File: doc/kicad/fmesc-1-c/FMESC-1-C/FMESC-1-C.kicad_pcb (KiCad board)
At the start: 2 copper layers, 14 x 21 mm, 33 parts, among them J1 Conn_01x02, J2 Conn_01x02, J3 Conn_01x02, J4 Conn_01x02, J5 Conn_01x02, J6 Conn_01x02, U1 FD6288Q

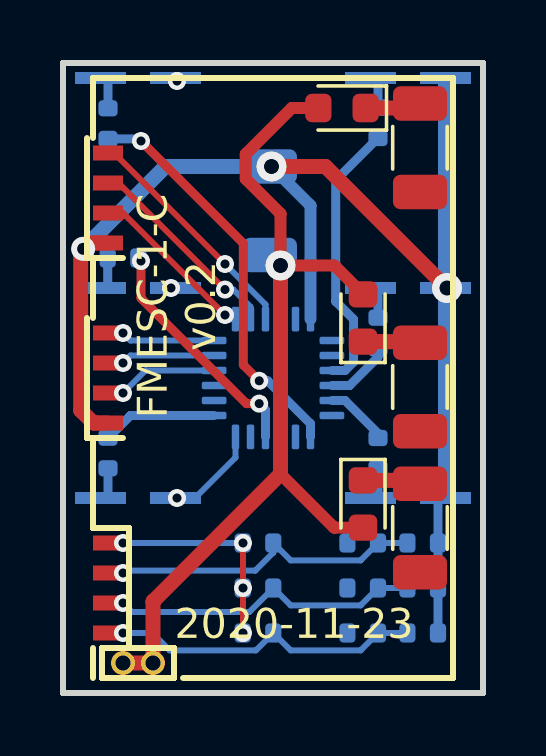
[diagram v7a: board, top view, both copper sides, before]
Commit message: doc/kicad: FMESC-1-C PCB clean and use FMPCBVDL-1
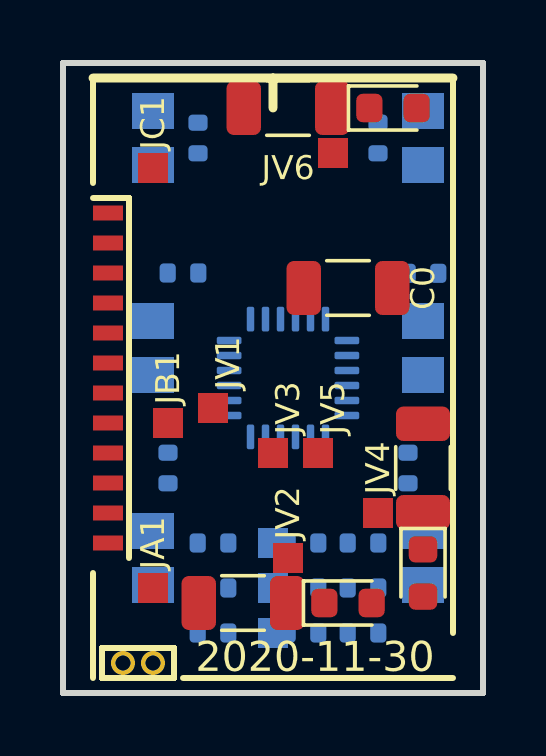
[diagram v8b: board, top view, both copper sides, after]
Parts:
- removed JC3: Conn_01x04, fmlibf:JS_4P_1.0mm
- added JA1: Conn_01x01, fmlibf:JS_1P_1x1mm, F.Cu at (116.5, 71.5)
- added JA2: Conn_01x01, fmlibf:JS_1P_1x1mm, B.Cu at (120.5, 73.0)
- added JB1: Conn_01x01, fmlibf:JS_1P_1x1mm, F.Cu at (117.0, 66.0)
- added JB2: Conn_01x01, fmlibf:JS_1P_1x1mm, B.Cu at (120.5, 71.5)
- added JM1: Conn_01x12, fmlibf:JS_12P_1.0mm, F.Cu at (115.0, 64.5)
- added JV1: Conn_01x01, fmlibf:JS_1P_1x1mm, F.Cu at (118.5, 65.5)
- added JV2: Conn_01x01, fmlibf:JS_1P_1x1mm, F.Cu at (121.0, 70.5)
- added JV3: Conn_01x01, fmlibf:JS_1P_1x1mm, F.Cu at (120.5, 67.0)
- added JV4: Conn_01x01, fmlibf:JS_1P_1x1mm, F.Cu at (124.0, 69.0)
- added JV5: Conn_01x01, fmlibf:JS_1P_1x1mm, F.Cu at (122.0, 67.0)
- added JV6: Conn_01x01, fmlibf:JS_1P_1x1mm, F.Cu at (122.5, 57.0)
- C0: moved to F.Cu
- J1, J2, J3, J4, J5, J6: footprint fmlibf:JS_2P_1.0mm_2 -> fmlibf:FMPCBVDL-1-S
- JC1: value Conn_01x04 -> Conn_01x01; footprint fmlibf:JS_4P_1.0mm -> fmlibf:JS_1P_1x1mm
- JC2: value Conn_01x04 -> Conn_01x01; footprint fmlibf:JS_4P_1.0mm -> fmlibf:JS_1P_1x1mm; moved to B.Cu
- moved D2 8.73 mm to (125.5, 71.0), turned to 270 degrees
- moved JC2 7.78 mm to (120.5, 70.0), turned to 0 degrees
- moved C1 6.41 mm to (119.5, 72.0), turned to 180 degrees
- moved C3 4.60 mm to (121.0, 55.5), turned to 180 degrees
- moved C0 3.66 mm to (123.0, 61.5), turned to 180 degrees
- moved R11 3.60 mm to (123.5, 73.0)
- moved R12 3.60 mm to (121.5, 73.0)
- moved R15 3.60 mm to (123.5, 70.0)
- moved R16 3.60 mm to (121.5, 70.0)
- moved R21 3.35 mm to (118.5, 73.0)
- moved R23 3.35 mm to (118.5, 70.0)
- moved D1 3.34 mm to (123.0, 72.0), turned to 0 degrees
- moved R6 3.04 mm to (118.0, 56.5)
- moved C2 2.70 mm to (125.5, 67.5), turned to 90 degrees
- moved R3 2.49 mm to (125.5, 61.0), turned to 0 degrees
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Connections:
- JC1 pad 1: GND -> /C1
- JC2 pad 1: GND -> Net-(JC2-Pad1)
- R12 pad 2: /A1 -> Net-(JA2-Pad1)
- R14 pad 2: /B1 -> Net-(JB2-Pad1)
- R16 pad 2: /C1 -> Net-(JC2-Pad1)
- U1 pad 1: /CAL1 -> /GLA
- U1 pad 14: Net-(C3-Pad1) -> Net-(JV5-Pad1)
- U1 pad 17: Net-(C2-Pad1) -> Net-(JV3-Pad1)
- U1 pad 2: /CBL1 -> /GLB
- U1 pad 20: Net-(C1-Pad1) -> Net-(JV1-Pad1)
- U1 pad 22: /CAH1 -> /GHA
- U1 pad 23: /CBH1 -> /GHB
- U1 pad 24: /CCH1 -> /GHC
- U1 pad 3: /CCL1 -> /GLC
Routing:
- net GND: track 46.3 -> 0.00 mm, vias 3 -> 0
- net +BATT: track 31.7 -> 0.00 mm, vias 1 -> 0
- net /CHG: track 13.5 -> 0.00 mm, vias 2 -> 0
- net /SA: track 10.5 -> 0.00 mm, vias 1 -> 0
- net /SB: track 10.4 -> 0.00 mm, vias 1 -> 0
- net /SC: track 10.4 -> 0.00 mm, vias 1 -> 0
- net /CLG: track 9.14 -> 0.00 mm
- net /BHG: track 7.83 -> 0.00 mm, vias 2 -> 0
- net /CCL1: track 7.83 -> 0.00 mm, vias 1 -> 0
- net /S0: track 7.00 -> 0.00 mm, vias 4 -> 0
- net /CBL1: track 6.77 -> 0.00 mm, vias 1 -> 0
- net /CAL1: track 5.72 -> 0.00 mm, vias 1 -> 0
- net /AHG: track 3.85 -> 0.00 mm
- net /CAH1: track 3.35 -> 0.00 mm, vias 1 -> 0
- net /CCH1: track 3.14 -> 0.00 mm, vias 1 -> 0
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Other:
- board text added: "2020-11-30"
- board text removed: "2020-11-23"
